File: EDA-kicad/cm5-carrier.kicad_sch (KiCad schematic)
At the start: 6 parts

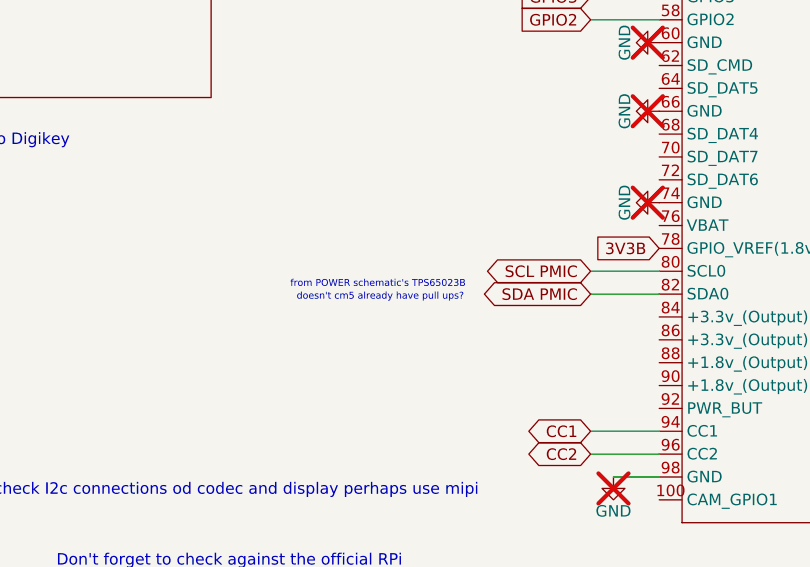
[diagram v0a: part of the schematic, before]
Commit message: remove redundant pull ups, connect charger and PMIC on single I2C bus
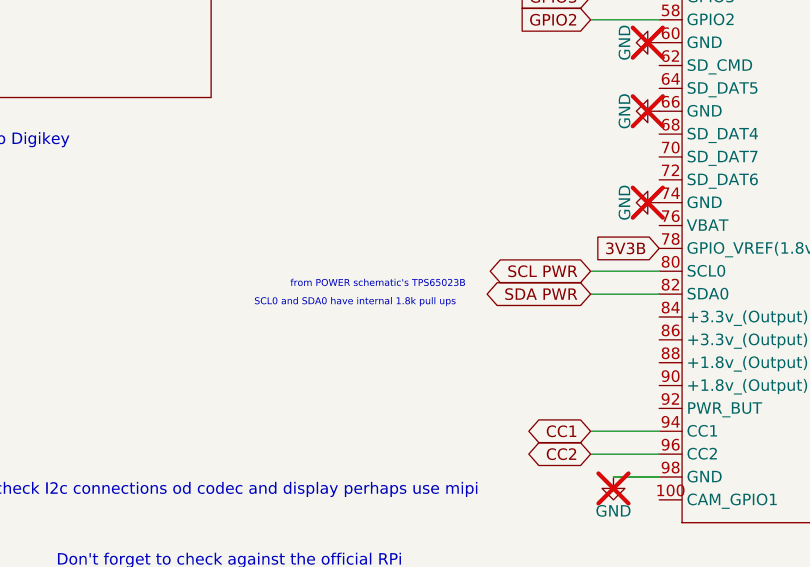
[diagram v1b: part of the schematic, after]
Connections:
- net SCL PMIC renamed SCL PWR
- net SDA PMIC renamed SDA PWR
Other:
- note added: "SCL0 and SDA0 have internal 1.8k pull ups"
- note removed: "doesn't cm5 already have pull ups?"
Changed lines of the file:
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@@
 		)
 	)
-	(text "doesn't cm5 already have pull ups?\n\n"
+	(text "SCL0 and SDA0 have internal 1.8k pull ups"
 		(exclude_from_sim no)
-		(at 212.852 176.276 0)
+		(at 210.058 176.276 0)
 		(effects
 			(font
@@
 		)
 	)
-	(global_label "SCL PMIC"
+	(global_label "SCL PWR"
 		(shape bidirectional)
 		(at 236.22 172.72 180)
@@
 		)
 		(property "Intersheetrefs" "${INTERSHEET_REFS}"
-			(at 223.0521 172.72 0)
+			(at 223.6569 172.72 0)
 			(effects
 				(font
@@
 		)
 	)
-	(global_label "SDA PMIC"
+	(global_label "SDA PWR"
 		(shape bidirectional)
 		(at 236.22 175.26 180)
@@
 		)
 		(property "Intersheetrefs" "${INTERSHEET_REFS}"
-			(at 222.9916 175.26 0)
+			(at 223.5964 175.26 0)
 			(effects
 				(font

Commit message: connect USB switch
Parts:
- C1, C2, C3, C4, R1: now fitted
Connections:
- net D+ renamed SYS D+
- net D- renamed SYS D-
